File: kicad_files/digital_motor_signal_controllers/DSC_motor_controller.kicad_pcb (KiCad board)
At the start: 4 copper layers, 106 x 108.4 mm, 106 parts, among them P1 PH_A, P2 PH_B, P3 PH_C, P4 SUPPLY, P5 GND, Q1 IRFS7730TRLPBF, Q2 IRFS7730TRLPBF, Q3 IRFS7730TRLPBF, Q4 IRFS7730TRLPBF, Q5 IRFS7730TRLPBF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

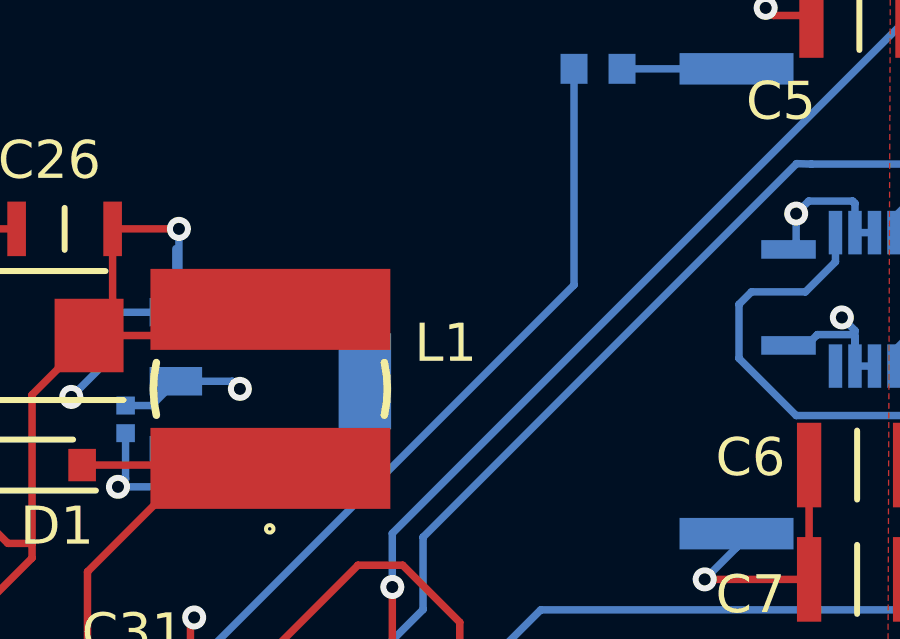
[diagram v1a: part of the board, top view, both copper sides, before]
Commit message: Code and PCB modifications
Adjustments to DSC motor controller PCB as well as BOMs
Nearly completed cannibalization of VESC code for the DSC motor control
application.
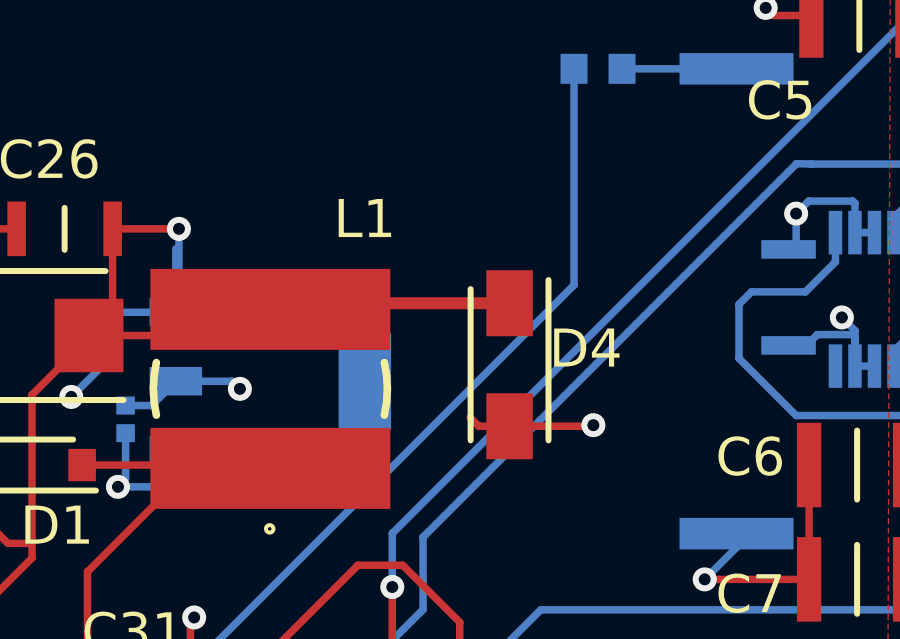
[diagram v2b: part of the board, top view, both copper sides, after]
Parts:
- added D4: TVS, SMAJ5.0A:DIOM5026X229N, F.Cu at (150.9, 89.2)
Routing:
- net +5V: track 69.6 -> 77.6 mm
- net GND: track 205.4 -> 209.7 mm, vias 41 -> 42
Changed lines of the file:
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@@
     (thickness 1.6)
     (drawings 19)
-    (tracks 951)
+    (tracks 958)
     (zones 0)
-    (modules 106)
+    (modules 107)
     (nets 151)
   )
@@
     (35 F.Paste user hide)
     (36 B.SilkS user hide)
-    (37 F.SilkS user hide)
+    (37 F.SilkS user)
     (38 B.Mask user hide)
     (39 F.Mask user hide)
@@
     (tags Inductor)
     (attr smd)
-    (fp_text reference L1 (at -5.842 1.524 180) (layer F.SilkS)
+    (fp_text reference L1 (at -3.147 5.648 180) (layer F.SilkS)
       (effects (font (size 1.27 1.27) (thickness 0.254)))
     )
@@
     )
   )
+  (module SMAJ5.0A:DIOM5026X229N (layer F.Cu)
+    (at 150.876 89.172 270)
+    (descr SMAJ5.0A)
+    (tags "TVS Diode (Uni-directional)")
+    (attr smd)
+    (fp_text reference D4 (at -0.526 -2.54 180) (layer F.SilkS)
+      (effects (font (size 1.27 1.27) (thickness 0.254)))
+    )
+    (fp_text value TVS (at 0 0 90) (layer F.SilkS) hide
+      (effects (font (size 1.27 1.27) (thickness 0.254)))
+    )
+    (fp_line (start -3.4 -1.645) (end 3.4 -1.645) (layer Dwgs.User) (width 0.05))
+    (fp_line (start 3.4 -1.645) (end 3.4 1.645) (layer Dwgs.User) (width 0.05))
+    (fp_line (start 3.4 1.645) (end -3.4 1.645) (layer Dwgs.User) (width 0.05))
+    (fp_line (start -3.4 1.645) (end -3.4 -1.645) (layer Dwgs.User) (width 0.05))
+    (fp_line (start -2.52 -1.298) (end 2.52 -1.298) (layer Dwgs.User) (width 0.1))
+    (fp_line (start 2.52 -1.298) (end 2.52 1.298) (layer Dwgs.User) (width 0.1))
+    (fp_line (start 2.52 1.298) (end -2.52 1.298) (layer Dwgs.User) (width 0.1))
+    (fp_line (start -2.52 1.298) (end -2.52 -1.298) (layer Dwgs.User) (width 0.1))
+    (fp_line (start -2.52 -0.522) (end -1.745 -1.298) (layer Dwgs.User) (width 0.1))
+    (fp_line (start 2.52 -1.298) (end -2.825 -1.298) (layer F.SilkS) (width 0.2))
+    (fp_line (start -2.52 1.298) (end 2.52 1.298) (layer F.SilkS) (width 0.2))
+    (pad 1 smd rect (at -2.05 0) (size 1.55 2.2) (layers F.Cu F.Paste F.Mask)
+      (net 2 +5V))
+    (pad 2 smd rect (at 2.05 0) (size 1.55 2.2) (layers F.Cu F.Paste F.Mask)
+      (net 1 GND))
+    (model "/home/matthew/Senior design/Models/Models_motor_control/LIB_SMAJ5.0A/SMAJ5.0A/3D/SMAJ5.0A.stp"
+      (at (xyz 0 0 0))
+      (scale (xyz 1 1 1))
+      (rotate (xyz 0 0 0))
+    )
+  )
   (gr_text "BIDOOF PLS" (at 122.35 72.95) (layer B.SilkS)
     (effects (font (size 1.5 1.5) (thickness 0.3)) (justify mirror))
@@
   (via (at 123.345 126.806) (size 0.8) (drill 0.4) (layers F.Cu B.Cu) (net 1))
   (segment (start 124.0435 127.5045) (end 123.345 126.806) (width 0.25) (layer F.Cu) (net 1))
+  (segment (start 149.851 91.222) (end 149.561 90.932) (width 0.25) (layer F.Cu) (net 1))
+  (segment (start 150.876 91.222) (end 149.851 91.222) (width 0.25) (layer F.Cu) (net 1))
+  (segment (start 150.876 91.222) (end 153.634 91.222) (width 0.25) (layer F.Cu) (net 1))
+  (via (at 153.67 91.186) (size 0.8) (drill 0.4) (layers F.Cu B.Cu) (net 1))
+  (segment (start 153.634 91.222) (end 153.67 91.186) (width 0.25) (layer F.Cu) (net 1))
   (segment (start 137.645 87.412) (end 136.859 88.198) (width 0.25) (layer F.Cu) (net 2) (status 30))
   (segment (start 137.645 84.642) (end 137.645 87.412) (width 0.25) (layer F.Cu) (net 2) (status 30))
@@
   (segment (start 125.615 83.602998) (end 124.525003 82.513001) (width 0.25) (layer F.Cu) (net 2))
   (segment (start 113.255 89.468) (end 111.391 87.604) (width 0.25) (layer F.Cu) (net 2))
+  (segment (start 143.107 87.122) (end 142.903 87.326) (width 0.25) (layer F.Cu) (net 2))
+  (segment (start 150.876 87.122) (end 143.107 87.122) (width 0.4) (layer F.Cu) (net 2))
   (segment (start 90.528 99.247) (end 90.325 99.45) (width 0.25) (layer B.Cu) (net 3) (status 30))
   (segment (start 91.9945 99.247) (end 90.528 99.247) (width 0.25) (layer B.Cu) (net 3) (status 30))

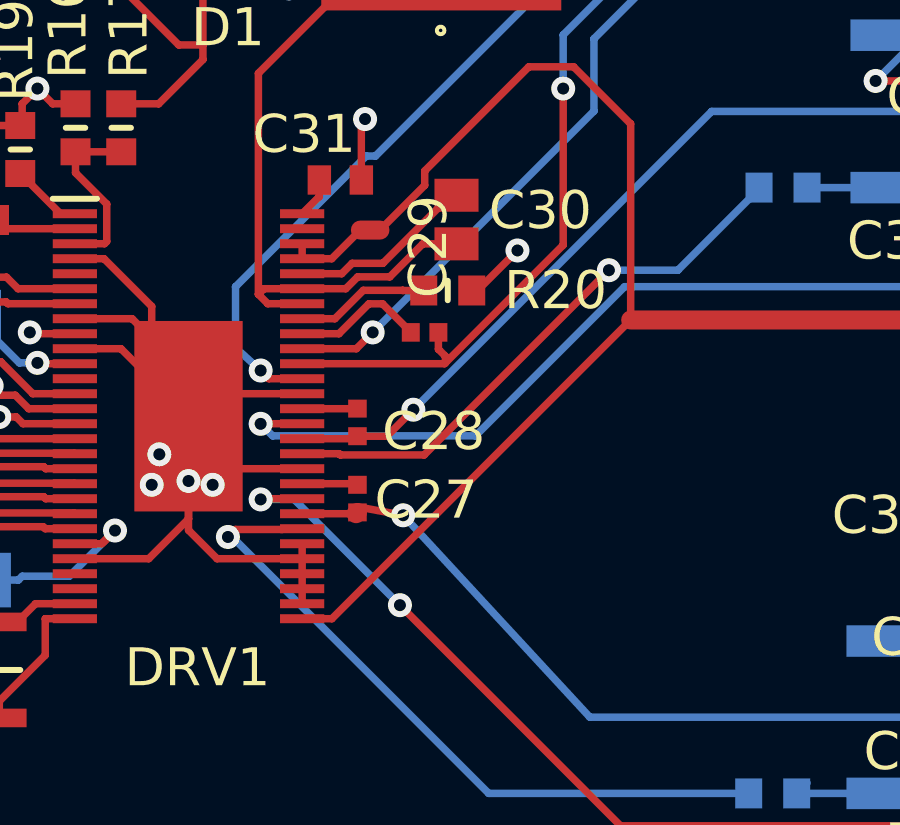
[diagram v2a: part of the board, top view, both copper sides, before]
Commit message: replaced 220nf resistor with component that fit, moved silkscreen around, updated BOM
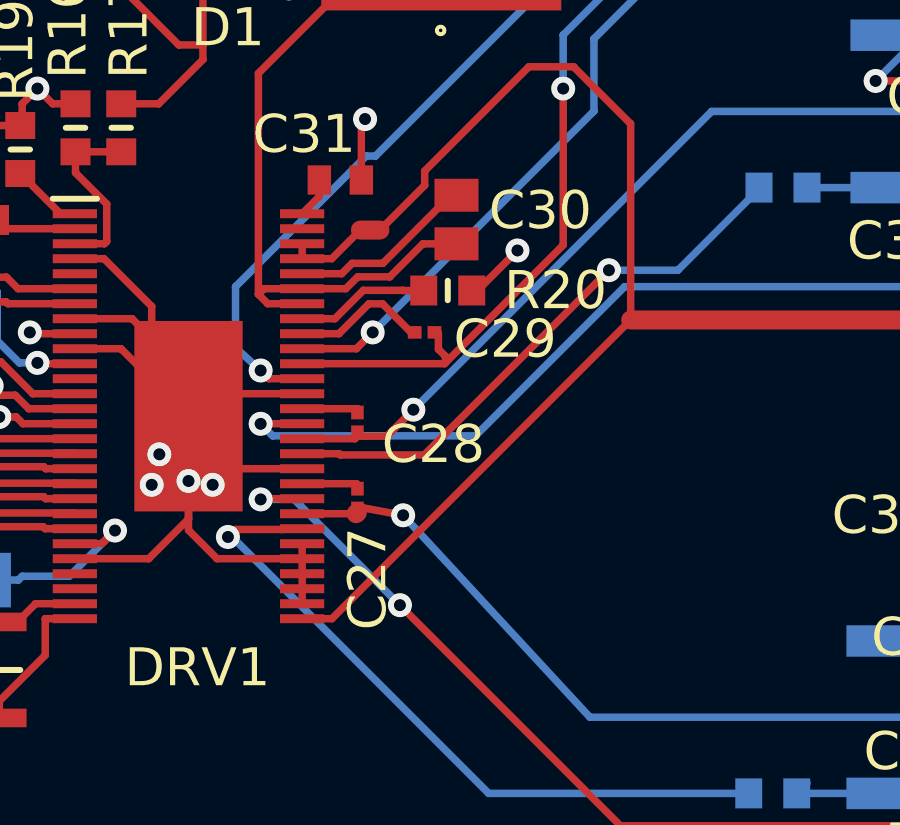
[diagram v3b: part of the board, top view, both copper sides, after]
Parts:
- C27, C28, C29: value 220n -> 220nf; footprint GRM155C91C105ME11J:CAPC1005X55N -> GRM033R61E224KE01D:CAPC0603X33N
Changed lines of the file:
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@@
-(kicad_pcb (version 20171130) (host pcbnew 5.1.4-e60b266~84~ubuntu19.04.1)
+(kicad_pcb (version 20171130) (host pcbnew 5.1.4+dfsg1-1)
   (general
     (thickness 1.6)
@@
   (layers
     (0 F.Cu signal)
-    (1 In1.Cu power)
-    (2 In2.Cu power)
-    (31 B.Cu signal)
+    (1 In1.Cu power hide)
+    (2 In2.Cu power hide)
+    (31 B.Cu signal hide)
     (32 B.Adhes user hide)
     (33 F.Adhes user hide)
@@
     )
   )
-  (module GRM155C91C105ME11J:CAPC1005X55N (layer F.Cu)
-    (at 142.347 104.708)
-    (descr GRM155)
-    (tags Capacitor)
-    (attr smd)
-    (fp_text reference C29 (at 0.127 -2.8575 90) (layer F.SilkS)
-      (effects (font (size 1.27 1.27) (thickness 0.254)))
-    )
-    (fp_text value 220n (at 0 0 180) (layer F.SilkS) hide
-      (effects (font (size 1.27 1.27) (thickness 0.254)))
-    )
-    (fp_line (start -0.5 0.25) (end -0.5 -0.25) (layer Dwgs.User) (width 0.1))
-    (fp_line (start 0.5 0.25) (end -0.5 0.25) (layer Dwgs.User) (width 0.1))
-    (fp_line (start 0.5 -0.25) (end 0.5 0.25) (layer Dwgs.User) (width 0.1))
-    (fp_line (start -0.5 -0.25) (end 0.5 -0.25) (layer Dwgs.User) (width 0.1))
-    (fp_line (start -0.91 0.46) (end -0.91 -0.46) (layer Dwgs.User) (width 0.05))
-    (fp_line (start 0.91 0.46) (end -0.91 0.46) (layer Dwgs.User) (width 0.05))
-    (fp_line (start 0.91 -0.46) (end 0.91 0.46) (layer Dwgs.User) (width 0.05))
-    (fp_line (start -0.91 -0.46) (end 0.91 -0.46) (layer Dwgs.User) (width 0.05))
-    (pad 2 smd rect (at 0.46 0) (size 0.6 0.62) (layers F.Cu F.Paste F.Mask)
-      (net 21 /Motor_Driver/SH_A))
-    (pad 1 smd rect (at -0.46 0) (size 0.6 0.62) (layers F.Cu F.Paste F.Mask)
-      (net 22 "Net-(C29-Pad1)"))
-    (model "/home/matthew/Senior design/Models/Models_motor_control/LIB_GRM155C81C105ME11J/GRM155C81C105ME11J/3D/GRM155C81C105ME11J.stp"
-      (at (xyz 0 0 0))
-      (scale (xyz 1 1 1))
-      (rotate (xyz 0 0 0))
-    )
-  )
-  (module GRM155C91C105ME11J:CAPC1005X55N (layer F.Cu)
-    (at 140.109 107.708 270)
-    (descr GRM155)
-    (tags Capacitor)
-    (attr smd)
-    (fp_text reference C28 (at 0.302 -2.54) (layer F.SilkS)
-      (effects (font (size 1.27 1.27) (thickness 0.254)))
-    )
-    (fp_text value 220n (at 0 0 270) (layer F.SilkS) hide
-      (effects (font (size 1.27 1.27) (thickness 0.254)))
-    )
-    (fp_line (start -0.5 0.25) (end -0.5 -0.25) (layer Dwgs.User) (width 0.1))
-    (fp_line (start 0.5 0.25) (end -0.5 0.25) (layer Dwgs.User) (width 0.1))
-    (fp_line (start 0.5 -0.25) (end 0.5 0.25) (layer Dwgs.User) (width 0.1))
-    (fp_line (start -0.5 -0.25) (end 0.5 -0.25) (layer Dwgs.User) (width 0.1))
-    (fp_line (start -0.91 0.46) (end -0.91 -0.46) (layer Dwgs.User) (width 0.05))
-    (fp_line (start 0.91 0.46) (end -0.91 0.46) (layer Dwgs.User) (width 0.05))
-    (fp_line (start 0.91 -0.46) (end 0.91 0.46) (layer Dwgs.User) (width 0.05))
-    (fp_line (start -0.91 -0.46) (end 0.91 -0.46) (layer Dwgs.User) (width 0.05))
-    (pad 2 smd rect (at 0.46 0 270) (size 0.6 0.62) (layers F.Cu F.Paste F.Mask)
-      (net 20 /Motor_Driver/SH_B))
-    (pad 1 smd rect (at -0.46 0 270) (size 0.6 0.62) (layers F.Cu F.Paste F.Mask)
-      (net 19 "Net-(C28-Pad1)"))
-    (model "/home/matthew/Senior design/Models/Models_motor_control/LIB_GRM155C81C105ME11J/GRM155C81C105ME11J/3D/GRM155C81C105ME11J.stp"
-      (at (xyz 0 0 0))
-      (scale (xyz 1 1 1))
-      (rotate (xyz 0 0 0))
-    )
-  )
-  (module GRM155C91C105ME11J:CAPC1005X55N (layer F.Cu)
-    (at 140.109 110.248 270)
-    (descr GRM155)
-    (tags Capacitor)
-    (attr smd)
-    (fp_text reference C27 (at 0.048 -2.286) (layer F.SilkS)
-      (effects (font (size 1.27 1.27) (thickness 0.254)))
-    )
-    (fp_text value 220n (at 0 0 270) (layer F.SilkS) hide
-      (effects (font (size 1.27 1.27) (thickness 0.254)))
-    )
-    (fp_line (start -0.5 0.25) (end -0.5 -0.25) (layer Dwgs.User) (width 0.1))
-    (fp_line (start 0.5 0.25) (end -0.5 0.25) (layer Dwgs.User) (width 0.1))
-    (fp_line (start 0.5 -0.25) (end 0.5 0.25) (layer Dwgs.User) (width 0.1))
-    (fp_line (start -0.5 -0.25) (end 0.5 -0.25) (layer Dwgs.User) (width 0.1))
-    (fp_line (start -0.91 0.46) (end -0.91 -0.46) (layer Dwgs.User) (width 0.05))
-    (fp_line (start 0.91 0.46) (end -0.91 0.46) (layer Dwgs.User) (width 0.05))
-    (fp_line (start 0.91 -0.46) (end 0.91 0.46) (layer Dwgs.User) (width 0.05))
-    (fp_line (start -0.91 -0.46) (end 0.91 -0.46) (layer Dwgs.User) (width 0.05))
-    (pad 2 smd rect (at 0.46 0 270) (size 0.6 0.62) (layers F.Cu F.Paste F.Mask)
-      (net 17 /Motor_Driver/SH_C))
-    (pad 1 smd rect (at -0.46 0 270) (size 0.6 0.62) (layers F.Cu F.Paste F.Mask)
-      (net 18 "Net-(C27-Pad1)"))
-    (model "/home/matthew/Senior design/Models/Models_motor_control/LIB_GRM155C81C105ME11J/GRM155C81C105ME11J/3D/GRM155C81C105ME11J.stp"
-      (at (xyz 0 0 0))
-      (scale (xyz 1 1 1))
-      (rotate (xyz 0 0 0))
-    )
-  )
   (module GRM155C91C105ME11J:CAPC1005X55N (layer B.Cu)
     (at 138.077 90.992 270)
@@
       (at (xyz 0 0 0))
       (scale (xyz 1 1 1))
+      (rotate (xyz 0 0 0))
+    )
+  )
+  (module GRM033R61E224KE01D:CAPC0603X33N (layer F.Cu)
+    (at 140.109 110.248 270)
+    (descr "GRM03_0.03 L=0.6mm W=0.3mm T=0.3mm")
+    (tags Capacitor)
+    (attr smd)
+    (fp_text reference C27 (at 2.672 -0.341 90) (layer F.SilkS)
+      (effects (font (size 1.27 1.27) (thickness 0.254)))
+    )
+    (fp_text value 220nf (at 0 0 90) (layer F.SilkS) hide
+      (effects (font (size 1.27 1.27) (thickness 0.254)))
+    )
+    (fp_line (start -0.71 -0.36) (end 0.71 -0.36) (layer Dwgs.User) (width 0.05))
+    (fp_line (start 0.71 -0.36) (end 0.71 0.36) (layer Dwgs.User) (width 0.05))
+    (fp_line (start 0.71 0.36) (end -0.71 0.36) (layer Dwgs.User) (width 0.05))
+    (fp_line (start -0.71 0.36) (end -0.71 -0.36) (layer Dwgs.User) (width 0.05))
+    (fp_line (start -0.3 -0.15) (end 0.3 -0.15) (layer Dwgs.User) (width 0.1))
+    (fp_line (start 0.3 -0.15) (end 0.3 0.15) (layer Dwgs.User) (width 0.1))
+    (fp_line (start 0.3 0.15) (end -0.3 0.15) (layer Dwgs.User) (width 0.1))
+    (fp_line (start -0.3 0.15) (end -0.3 -0.15) (layer Dwgs.User) (width 0.1))
+    (pad 1 smd rect (at -0.33 0) (size 0.42 0.46) (layers F.Cu F.Paste F.Mask)
+      (net 18 "Net-(C27-Pad1)"))
+    (pad 2 smd rect (at 0.33 0) (size 0.42 0.46) (layers F.Cu F.Paste F.Mask)
+      (net 17 /Motor_Driver/SH_C))
+    (model "/home/matthew/Senior design/Models/Models_motor_control/LIB_GRM033R61E224KE01D/GRM033R61E224KE01D/3D/GRM033R61E224KE01D.stp"
+      (at (xyz 0 0 0))
+      (scale (xyz 1 1 1))
+      (rotate (xyz 0 0 0))
+    )
+  )
+  (module GRM033R61E224KE01D:CAPC0603X33N (layer F.Cu)
+    (at 140.109 107.708 270)
+    (descr "GRM03_0.03 L=0.6mm W=0.3mm T=0.3mm")
+    (tags Capacitor)
+    (attr smd)
+    (fp_text reference C28 (at 0.732 -2.531 180) (layer F.SilkS)
+      (effects (font (size 1.27 1.27) (thickness 0.254)))
+    )
+    (fp_text value 220nf (at 0 0 90) (layer F.SilkS) hide
+      (effects (font (size 1.27 1.27) (thickness 0.254)))
+    )
+    (fp_line (start -0.3 0.15) (end -0.3 -0.15) (layer Dwgs.User) (width 0.1))
+    (fp_line (start 0.3 0.15) (end -0.3 0.15) (layer Dwgs.User) (width 0.1))
+    (fp_line (start 0.3 -0.15) (end 0.3 0.15) (layer Dwgs.User) (width 0.1))
+    (fp_line (start -0.3 -0.15) (end 0.3 -0.15) (layer Dwgs.User) (width 0.1))
+    (fp_line (start -0.71 0.36) (end -0.71 -0.36) (layer Dwgs.User) (width 0.05))
+    (fp_line (start 0.71 0.36) (end -0.71 0.36) (layer Dwgs.User) (width 0.05))
+    (fp_line (start 0.71 -0.36) (end 0.71 0.36) (layer Dwgs.User) (width 0.05))
+    (fp_line (start -0.71 -0.36) (end 0.71 -0.36) (layer Dwgs.User) (width 0.05))
+    (pad 2 smd rect (at 0.33 0) (size 0.42 0.46) (layers F.Cu F.Paste F.Mask)
+      (net 20 /Motor_Driver/SH_B))
+    (pad 1 smd rect (at -0.33 0) (size 0.42 0.46) (layers F.Cu F.Paste F.Mask)
+      (net 19 "Net-(C28-Pad1)"))
+    (model "/home/matthew/Senior design/Models/Models_motor_control/LIB_GRM033R61E224KE01D/GRM033R61E224KE01D/3D/GRM033R61E224KE01D.stp"
+      (at (xyz 0 0 0))
+      (scale (xyz 1 1 1))
+      (rotate (xyz 0 0 0))
+    )
+  )
+  (module GRM033R61E224KE01D:CAPC0603X33N (layer F.Cu)
+    (at 142.347 104.708)
+    (descr "GRM03_0.03 L=0.6mm W=0.3mm T=0.3mm")
+    (tags Capacitor)
+    (attr smd)
+    (fp_text reference C29 (at 2.683 0.222) (layer F.SilkS)
+      (effects (font (size 1.27 1.27) (thickness 0.254)))
+    )
+    (fp_text value 220nf (at 0 0) (layer F.SilkS) hide
+      (effects (font (size 1.27 1.27) (thickness 0.254)))
+    )
+    (fp_line (start -0.71 -0.36) (end 0.71 -0.36) (layer Dwgs.User) (width 0.05))
+    (fp_line (start 0.71 -0.36) (end 0.71 0.36) (layer Dwgs.User) (width 0.05))
+    (fp_line (start 0.71 0.36) (end -0.71 0.36) (layer Dwgs.User) (width 0.05))
+    (fp_line (start -0.71 0.36) (end -0.71 -0.36) (layer Dwgs.User) (width 0.05))
+    (fp_line (start -0.3 -0.15) (end 0.3 -0.15) (layer Dwgs.User) (width 0.1))
+    (fp_line (start 0.3 -0.15) (end 0.3 0.15) (layer Dwgs.User) (width 0.1))
+    (fp_line (start 0.3 0.15) (end -0.3 0.15) (layer Dwgs.User) (width 0.1))
+    (fp_line (start -0.3 0.15) (end -0.3 -0.15) (layer Dwgs.User) (width 0.1))
+    (pad 1 smd rect (at -0.33 0 90) (size 0.42 0.46) (layers F.Cu F.Paste F.Mask)
+      (net 22 "Net-(C29-Pad1)"))
+    (pad 2 smd rect (at 0.33 0 90) (size 0.42 0.46) (layers F.Cu F.Paste F.Mask)
+      (net 21 /Motor_Driver/SH_A))
+    (model "/home/matthew/Senior design/Models/Models_motor_control/LIB_GRM033R61E224KE01D/GRM033R61E224KE01D/3D/GRM033R61E224KE01D.stp"
+      (at (xyz 0 0 0))
+      (scale (xyz 1 1 1))
